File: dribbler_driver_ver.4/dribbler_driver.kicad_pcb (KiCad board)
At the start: 2 copper layers, 79.8 x 34.9 mm, 101 parts, among them J1 Conn_01x04_Pin, J3 Conn_01x02_MountingPin, J4 Conn_01x02_MountingPin, J5 Conn_01x02_Pin, J6 Conn_01x08_Socket, Q1 WSD4070DN, Q10 WSD4070DN, Q2 WSD4070DN, Q5 WSD4070DN, Q6 WSD4070DN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

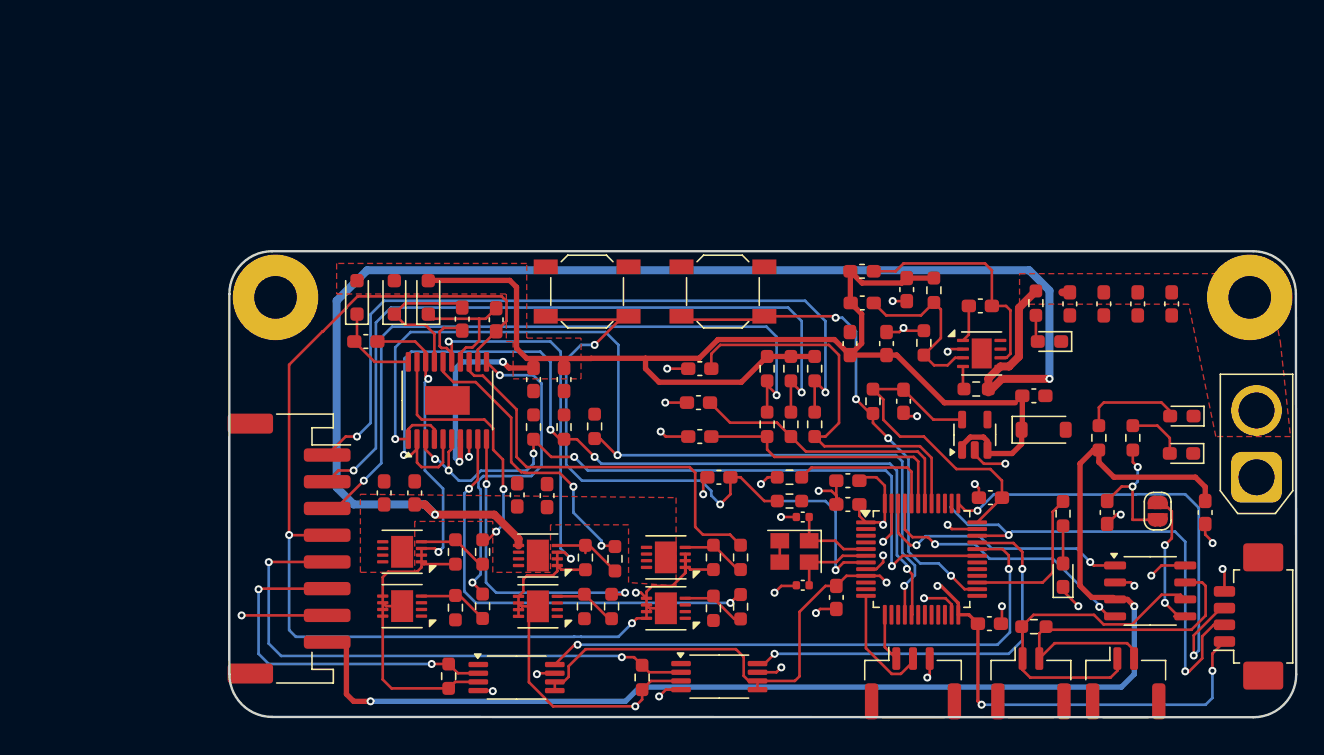
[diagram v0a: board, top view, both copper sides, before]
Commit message: updated pcb (GND network unprocessed)
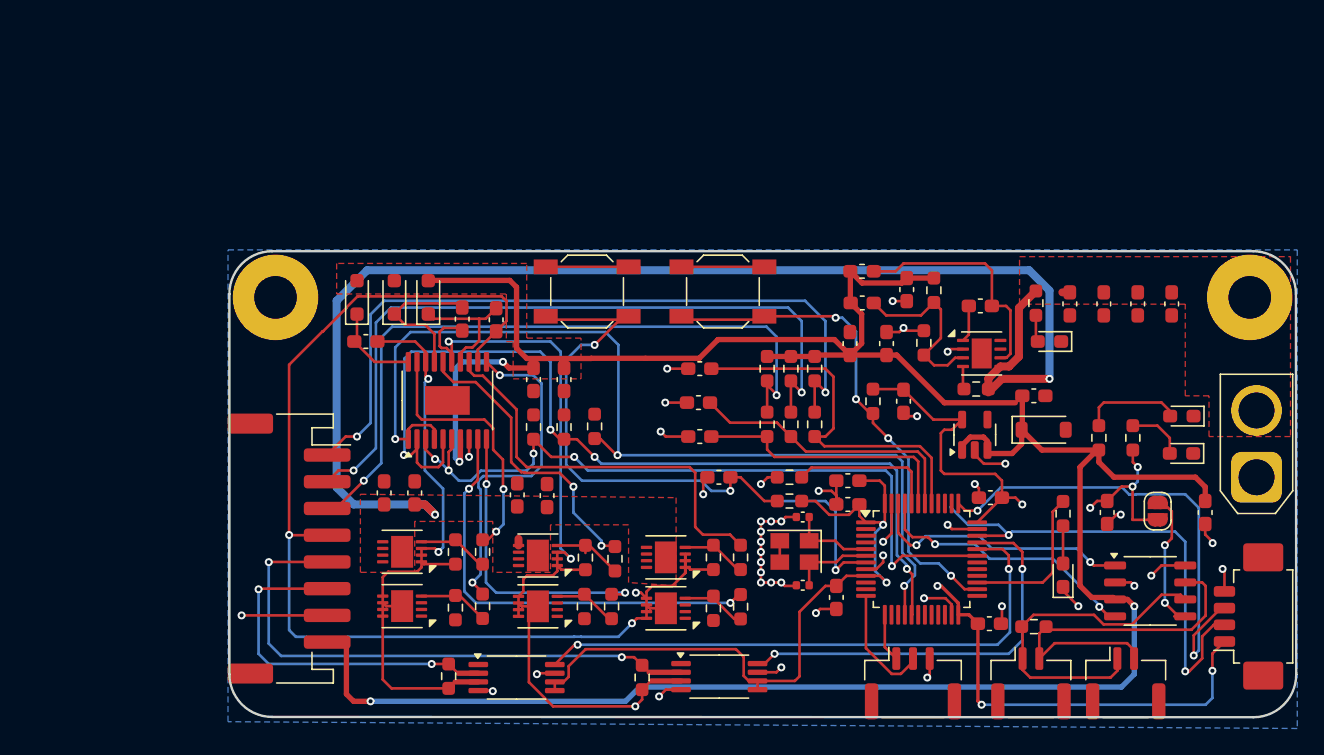
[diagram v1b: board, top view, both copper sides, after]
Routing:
- net GND: track 65.3 -> 84.8 mm, vias 33 -> 42
- net +3.3V: track 111.9 -> 121.5 mm, vias 7 -> 9
- net +24V: track 107.9 -> 100.9 mm
- net Net-(U1-PB5): track 31.4 -> 27.7 mm
- net +5V: track 202.2 -> 200.1 mm
- net NRST: track 39.8 -> 38.7 mm
- added copper zone on B.Cu, net +3.3V

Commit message: updated RY8411 footprint
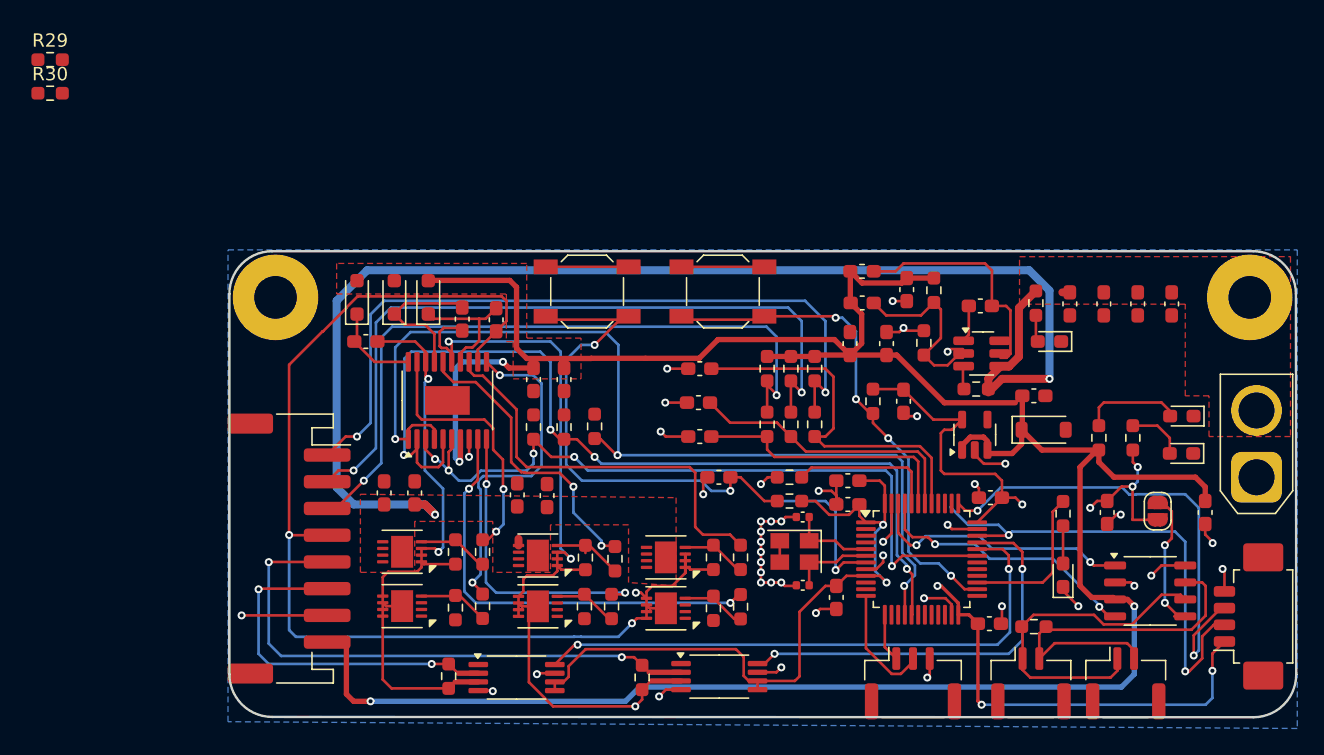
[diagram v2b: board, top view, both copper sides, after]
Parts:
- added R29: 10kΩ, Resistor_SMD:R_0603_1608Metric_Pad0.98x0.95mm_HandSolder, F.Cu at (1.68, 0.76)
- added R30: 10kΩ, Resistor_SMD:R_0603_1608Metric_Pad0.98x0.95mm_HandSolder, F.Cu at (1.68, 3.27)
- RY8411: footprint Package_DFN_QFN:DFN-8-1EP_3x3mm_P0.65mm_EP1.5x2.25mm -> Package_TO_SOT_SMD:SOT-23-6_Handsoldering

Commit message: footprint RY8411 updated
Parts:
- removed the R29 at (1.68, 0.76)
- removed the R30 at (1.68, 3.27)
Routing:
- net Net-(RY8411-SW): track 17.6 -> 14.8 mm
- net Net-(RY8411-EN): track 1.97 -> 4.14 mm
